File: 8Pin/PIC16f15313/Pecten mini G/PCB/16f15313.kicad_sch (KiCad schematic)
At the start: 17 parts, among them J1 JACK DC, J2 USB_B, J3 TERMINAL BLOCK, J4 POWER HEADERS, J5 Conn_02x04_Odd_Even, J6 Conn_02x04_Odd_Even, J7 ICSP, SW1 RESET, SW2 CONTROL

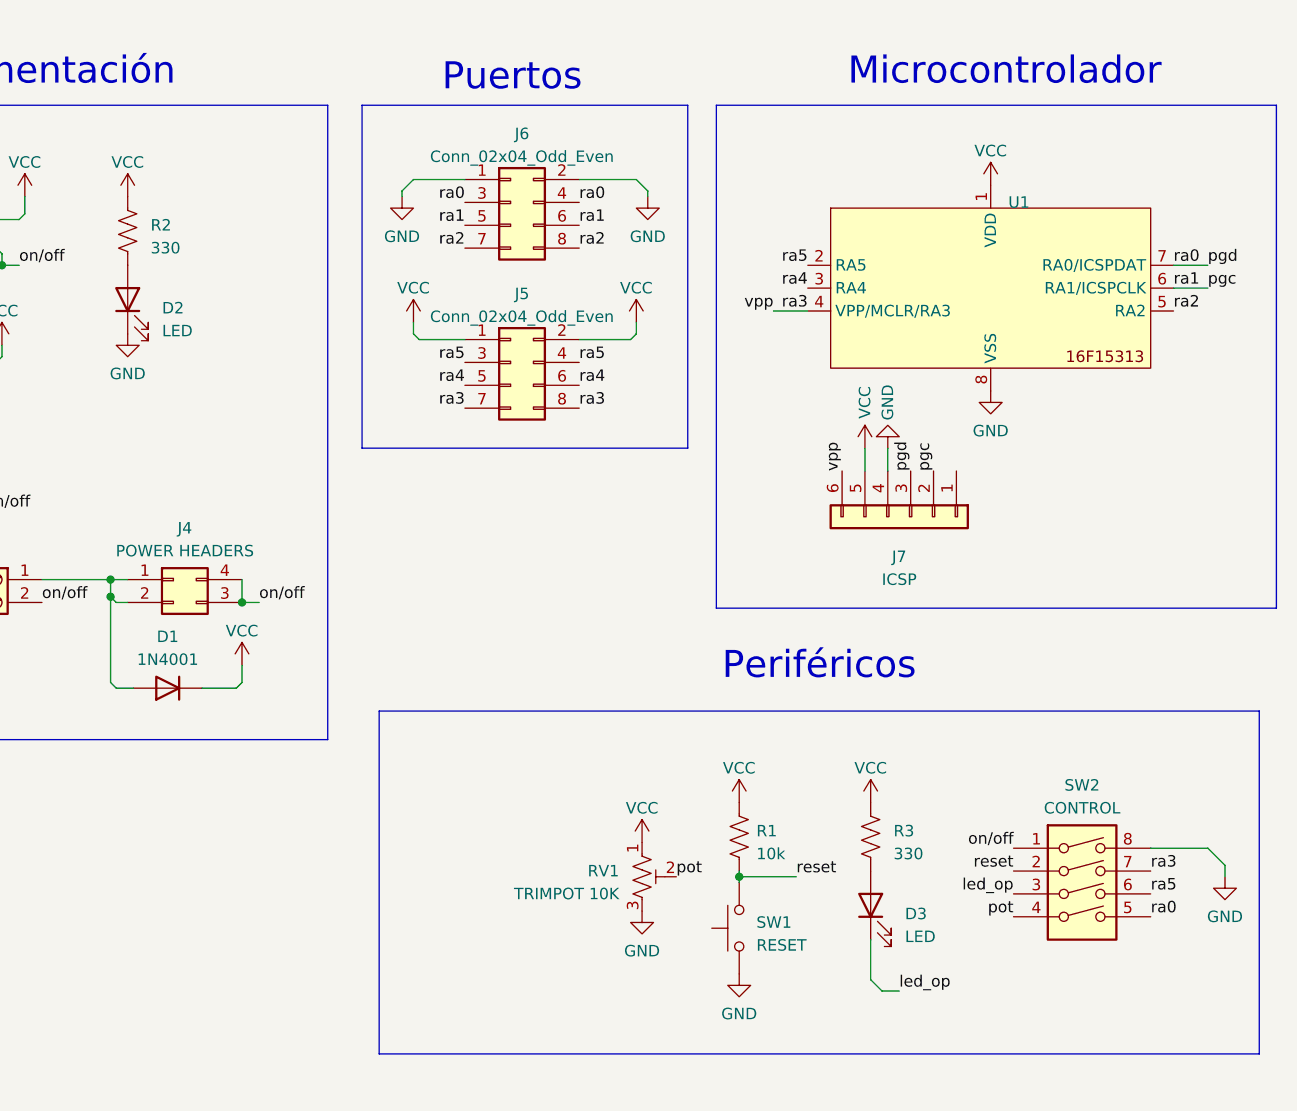
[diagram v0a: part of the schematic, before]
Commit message: Ruteo de la tarjeta Pecten Mini
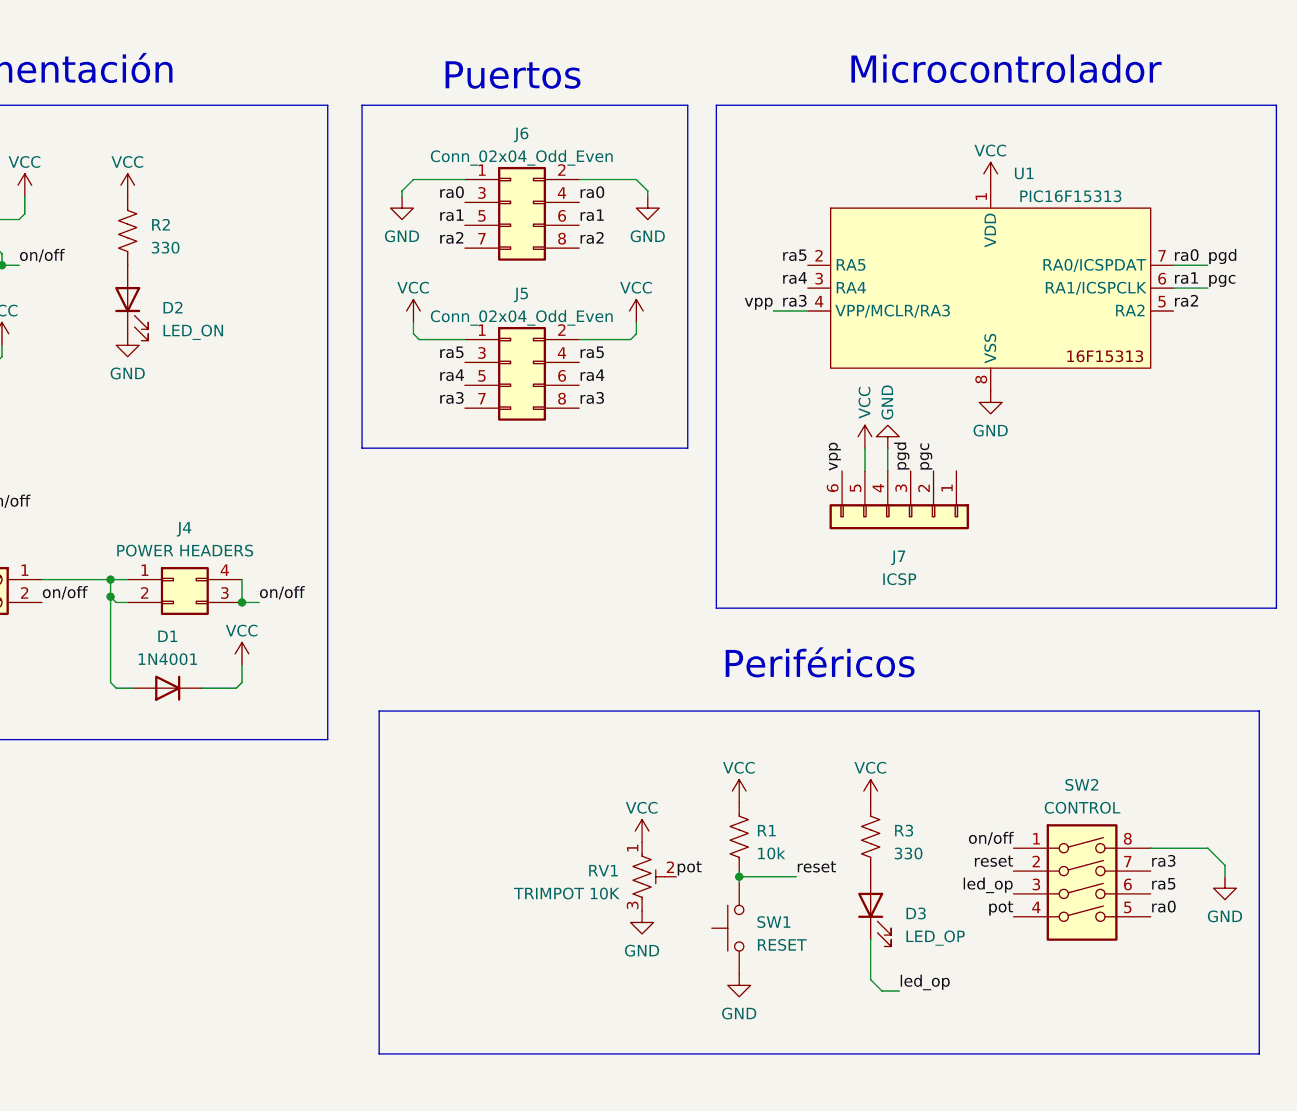
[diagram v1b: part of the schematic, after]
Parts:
- D2: value LED -> LED_ON
- D3: value LED -> LED_OP
- J1: footprint Connector_BarrelJack:BarrelJack_Horizontal -> Connector_BarrelJack:BarrelJack_Kycon_KLDX-0202-xC_Horizontal
- RV1: footprint (none) -> Potentiometer_THT:Potentiometer_Vishay_T73YP_Vertical
- U1: value ~ -> PIC16F15313
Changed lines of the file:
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@@
       (effects (font (size 1.27 1.27)) (justify right))
     )
-    (property "Value" "LED" (at 149.86 129.8575 90)
+    (property "Value" "LED_OP" (at 149.86 129.8575 90)
       (effects (font (size 1.27 1.27)) (justify right))
     )
@@
       (effects (font (size 1.27 1.27)) (justify right))
     )
-    (property "Value" "LED" (at 67.31 62.5475 90)
+    (property "Value" "LED_ON" (at 67.31 62.5475 90)
       (effects (font (size 1.27 1.27)) (justify right))
     )
@@
   (symbol (lib_id "MGV:PIC16F15313") (at 159.385 57.785 0) (unit 1)
     (in_bom yes) (on_board yes) (dnp no) (fields_autoplaced)
-    (property "Reference" "U1" (at 161.3409 48.26 0)
+    (property "Reference" "U1" (at 161.925 45.085 0)
       (effects (font (size 1.27 1.27)) (justify left))
     )
-    (property "Value" "~" (at 159.385 57.785 0)
+    (property "Value" "PIC16F15313" (at 168.275 47.625 0)
       (effects (font (size 1.27 1.27)))
     )
@@
       (effects (font (size 1.27 1.27)))
     )
-    (property "Footprint" "Connector_BarrelJack:BarrelJack_Horizontal" (at 40.64 53.721 0)
+    (property "Footprint" "Connector_BarrelJack:BarrelJack_Kycon_KLDX-0202-xC_Horizontal" (at 40.64 53.721 0)
       (effects (font (size 1.27 1.27)) hide)
     )
@@
       (effects (font (size 1.27 1.27)) (justify right))
     )
-    (property "Footprint" "" (at 120.65 123.19 0)
-      (effects (font (size 1.27 1.27)) hide)
-    )
+    (property "Footprint" "Potentiometer_THT:Potentiometer_Vishay_T73YP_Vertical" (at 120.65 123.19 0)
+      (effects (font (size 1.27 1.27)) hide)
+    )
